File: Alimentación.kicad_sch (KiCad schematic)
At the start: 1 part, among them IC1 LDO40LPURY

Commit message: He corregido los errores de la tarea 2 y he añadido los condensadores de desacople.
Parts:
- added C4(desacople)2, C4(desacople)3: 100n, Capacitor_SMD:C_0805_2012Metric, symbol Device:C
- added J1: Conn_01x02_Pin, Connector_PinHeader_1.00mm:PinHeader_1x02_P1.00mm_Horizontal, symbol Connector:Conn_01x02_Pin
- IC1: footprint SON95P300X300X90-7N-D -> Package_DFN_QFN:DFN-6-1EP_3x3mm_P0.95mm_EP1.7x2.6mm; now left out of the parts list
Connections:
- net GND: now also J1.2 (Pin_2); no longer IC1.7 (GND_2)
- net VDD: now also IC1.4 (VOUT), C4(desacople)3.1; no longer IC1.3 (VIN)
- net at IC1.1 (GND_1): now also IC1.7 (GND_2), C4(desacople)2.2, C4(desacople)3.2
- new net: C4(desacople)2.1, IC1.3 (VIN)
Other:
- moved on the sheet: IC1

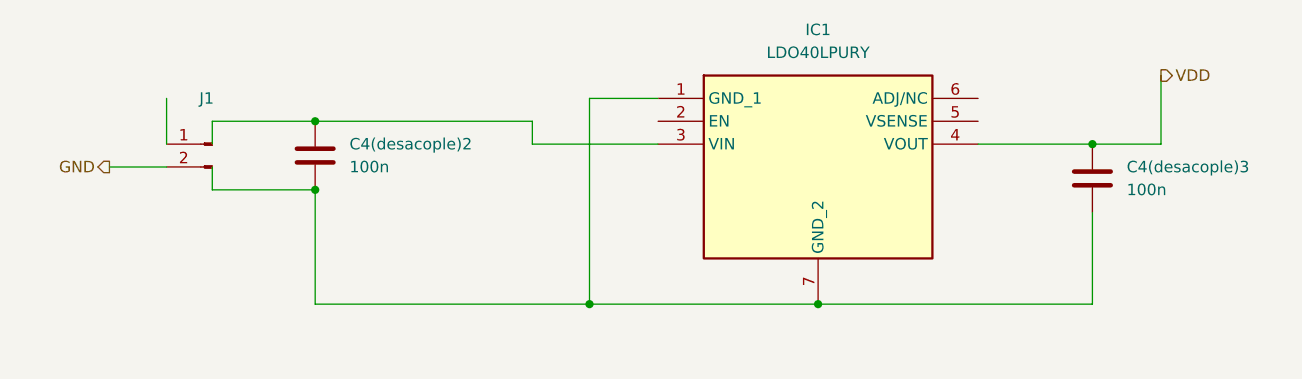
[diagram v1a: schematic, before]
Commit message: he añadido un conector de 4 pines a modo de sensor con un bus I2C, alimentación y gnd.
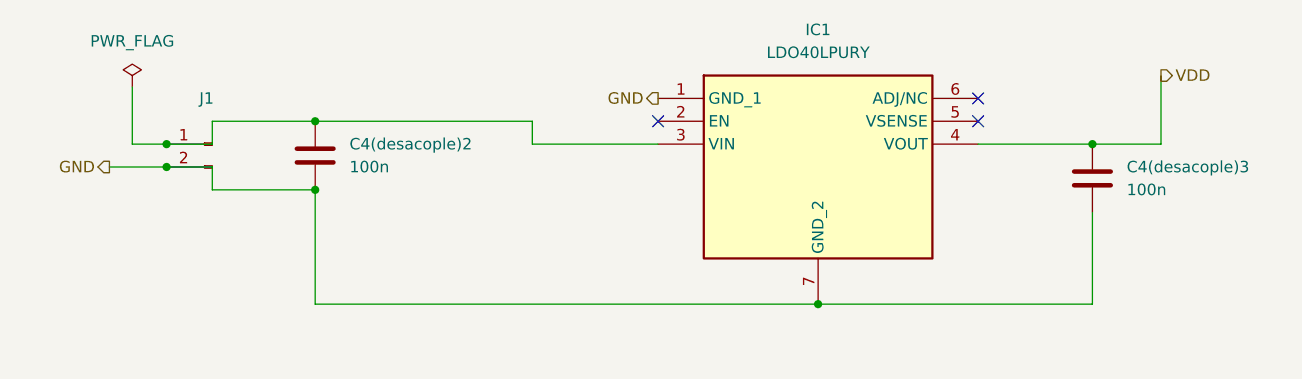
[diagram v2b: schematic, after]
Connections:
- net GND: now also C4(desacople)2.2, C4(desacople)3.2, IC1.1 (GND_1), IC1.7 (GND_2)
- net at C4(desacople)2.1, IC1.3 (VIN): now also J1.1 (Pin_1)
- no-connect marks 0 -> 3
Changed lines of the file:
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@@
 	(paper "A4")
 	(junction
-		(at 149.86 82.55)
+		(at 102.87 64.77)
 		(diameter 0)
 		(color 0 0 0 0)
@@
 	)
 	(junction
+		(at 102.87 67.31)
+		(diameter 0)
+		(color 0 0 0 0)
+	)
+	(junction
 		(at 119.38 69.85)
 		(diameter 0)
 		(color 0 0 0 0)
 	)
+	(no_connect
+		(at 157.48 62.23)
+	)
+	(no_connect
+		(at 193.04 62.23)
+	)
+	(no_connect
+		(at 193.04 59.69)
+	)
 	(wire
 		(pts
@@
 	(wire
 		(pts
-			(xy 107.95 64.77) (xy 107.95 62.23)
-		)
-		(stroke
-			(width 0)
-			(type default)
-		)
-	)
-	(wire
-		(pts
 			(xy 96.52 67.31) (xy 102.87 67.31)
 		)
@@
 	(wire
 		(pts
+			(xy 107.95 64.77) (xy 102.87 64.77)
+		)
+		(stroke
+			(width 0)
+			(type default)
+		)
+	)
+	(wire
+		(pts
 			(xy 143.51 64.77) (xy 157.48 64.77)
 		)
@@
 	(wire
 		(pts
-			(xy 157.48 59.69) (xy 149.86 59.69)
-		)
-		(stroke
-			(width 0)
-			(type default)
-		)
-	)
-	(wire
-		(pts
 			(xy 193.04 64.77) (xy 205.74 64.77)
 		)
@@
 	(wire
 		(pts
-			(xy 102.87 59.69) (xy 102.87 64.77)
-		)
-		(stroke
-			(width 0)
-			(type default)
-		)
-	)
-	(wire
-		(pts
-			(xy 149.86 82.55) (xy 175.26 82.55)
+			(xy 119.38 82.55) (xy 175.26 82.55)
 		)
 		(stroke
@@
 	(wire
 		(pts
-			(xy 149.86 59.69) (xy 149.86 82.55)
+			(xy 107.95 69.85) (xy 107.95 67.31)
+		)
+		(stroke
+			(width 0)
+			(type default)
+		)
+	)
+	(wire
+		(pts
+			(xy 99.06 58.42) (xy 99.06 64.77)
 		)
 		(stroke
@@
 	(wire
 		(pts
-			(xy 119.38 82.55) (xy 149.86 82.55)
-		)
-		(stroke
-			(width 0)
-			(type default)
-		)
-	)
-	(wire
-		(pts
-			(xy 107.95 67.31) (xy 107.95 69.85)
+			(xy 102.87 67.31) (xy 107.95 67.31)
+		)
+		(stroke
+			(width 0)
+			(type default)
+		)
+	)
+	(wire
+		(pts
+			(xy 107.95 62.23) (xy 107.95 64.77)
 		)
 		(stroke
@@
 		(pts
 			(xy 175.26 82.55) (xy 205.74 82.55)
+		)
+		(stroke
+			(width 0)
+			(type default)
+		)
+	)
+	(wire
+		(pts
+			(xy 99.06 64.77) (xy 102.87 64.77)
 		)
 		(stroke
@@
 		)
 	)
+	(hierarchical_label "GND"
+		(shape output)
+		(at 157.48 59.69 180)
+		(effects
+			(font
+				(size 1.27 1.27)
+			)
+			(justify right)
+		)
+	)
+	(symbol
+		(lib_id "power:PWR_FLAG")
+		(at 99.06 58.42 0)
+		(unit 1)
+		(body_style 1)
+		(exclude_from_sim no)
+		(in_bom yes)
+		(on_board yes)
+		(in_pos_files yes)
+		(dnp no)
+		(fields_autoplaced yes)
+		(property "Reference" "#FLG02"
+			(at 99.06 56.515 0)
+			(hide yes)
+			(show_name no)
+			(do_not_autoplace no)
+			(effects
+				(font
+					(size 1.27 1.27)
+				)
+			)
+		)
+		(property "Value" "PWR_FLAG"
+			(at 99.06 53.34 0)
+			(show_name no)
+			(do_not_autoplace no)
+			(effects
+				(font
+					(size 1.27 1.27)
+				)
+			)
+		)
+		(property "Footprint" ""
+			(at 99.06 58.42 0)
+			(hide yes)
+			(show_name no)
+			(do_not_autoplace no)
+			(effects
+				(font
+					(size 1.27 1.27)
+				)
+			)
+		)
+		(property "Datasheet" ""
+			(at 99.06 58.42 0)
+			(hide yes)
+			(show_name no)
+			(do_not_autoplace no)
+			(effects
+				(font
+					(size 1.27 1.27)
+				)
+			)
+		)
+		(property "Description" "Special symbol for telling ERC where power comes from"
+			(at 99.06 58.42 0)
+			(hide yes)
+			(show_name no)
+			(do_not_autoplace no)
+			(effects
+				(font
+					(size 1.27 1.27)
+				)
+			)
+		)
+		(pin "1"
+		)
+		(instances
+			(project "tarea2"
+				(path "/2450fa96-bfdf-43ef-9d5c-9c389bfd976a/857d8a4e-3168-4d95-8303-d58b522bce6b"
+					(reference "#FLG02")
+					(unit 1)
+				)
+			)
+		)
+	)
